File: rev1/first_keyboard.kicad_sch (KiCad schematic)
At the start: 79 parts, among them SW1 SW_Push, SW10 SW_Push, SW11 SW_Push, SW12 SW_Push, SW13 SW_Push, SW14 SW_Push, SW15 SW_Push, SW16 SW_Push, SW17 SW_Push, SW18 SW_Push, SW19 SW_Push, SW2 SW_Push, SW20 SW_Push, SW21 SW_Push, SW22 SW_Push, SW23 SW_Push, SW24 SW_Push, SW25 SW_Push, SW26 SW_Push, SW27 SW_Push, SW28 SW_Push, SW29 SW_Push, SW3 SW_Push, SW30 SW_Push, SW31 SW_Push, SW32 SW_Push, SW33 SW_Push, SW34 SW_Push, SW35 SW_Push, SW37 SW_Push, SW38 SW_Push, SW39 SW_Push, SW4 SW_Push, SW40 SW_Push, SW5 SW_Push, SW6 SW_Push, SW7 SW_Push, SW8 SW_Push, SW9 SW_Push, U1 RP2040

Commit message: feat: change rasp pico
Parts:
- removed U1: RP2040, Package_DFN_QFN:QFN-56-1EP_7x7mm_P0.4mm_EP3.2x3.2mm, symbol MCU_RaspberryPi:RP2040
- added U1: Pico, RPi_Pico:RPi_Pico_SMD_TH, symbol RPi_Pico:Pico

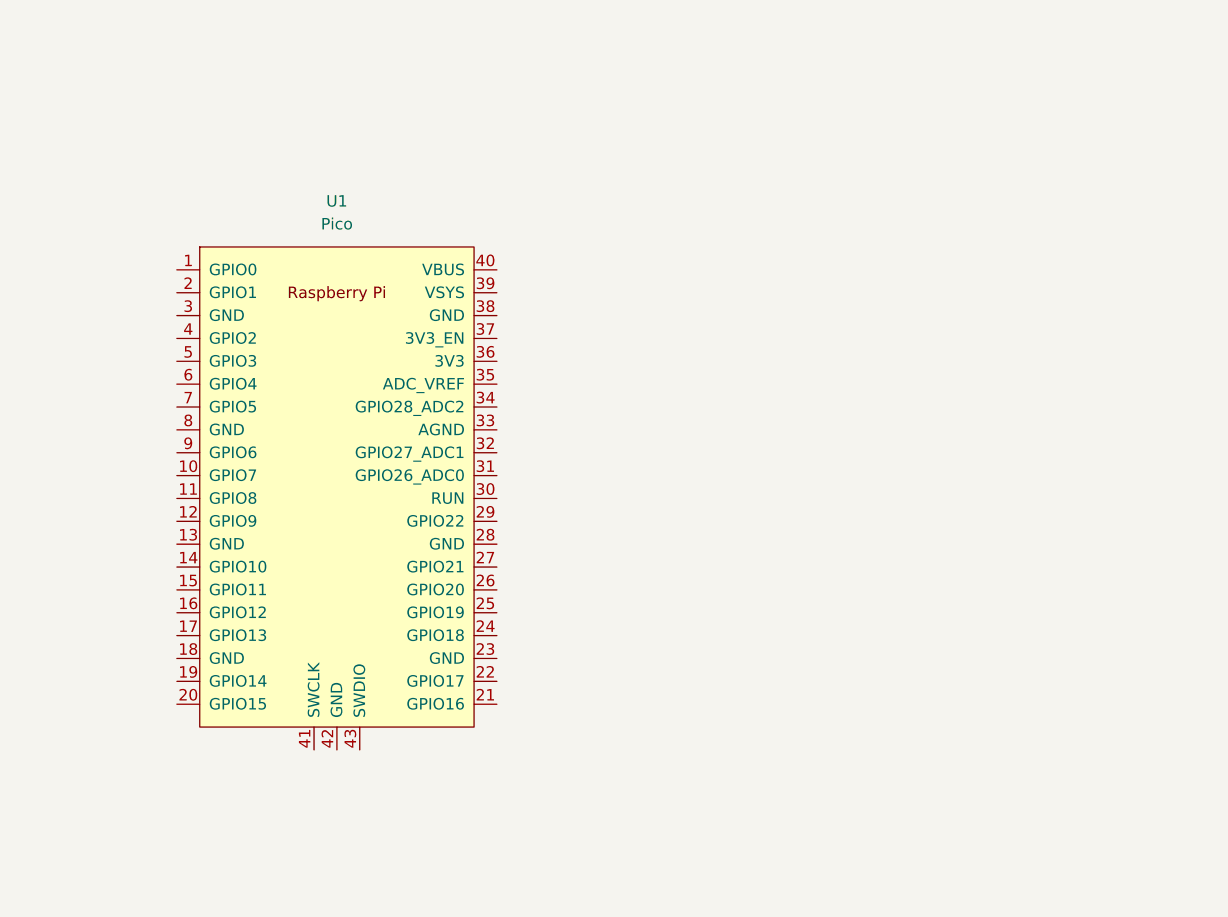
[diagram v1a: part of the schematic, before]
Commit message: feat: picoに配線した
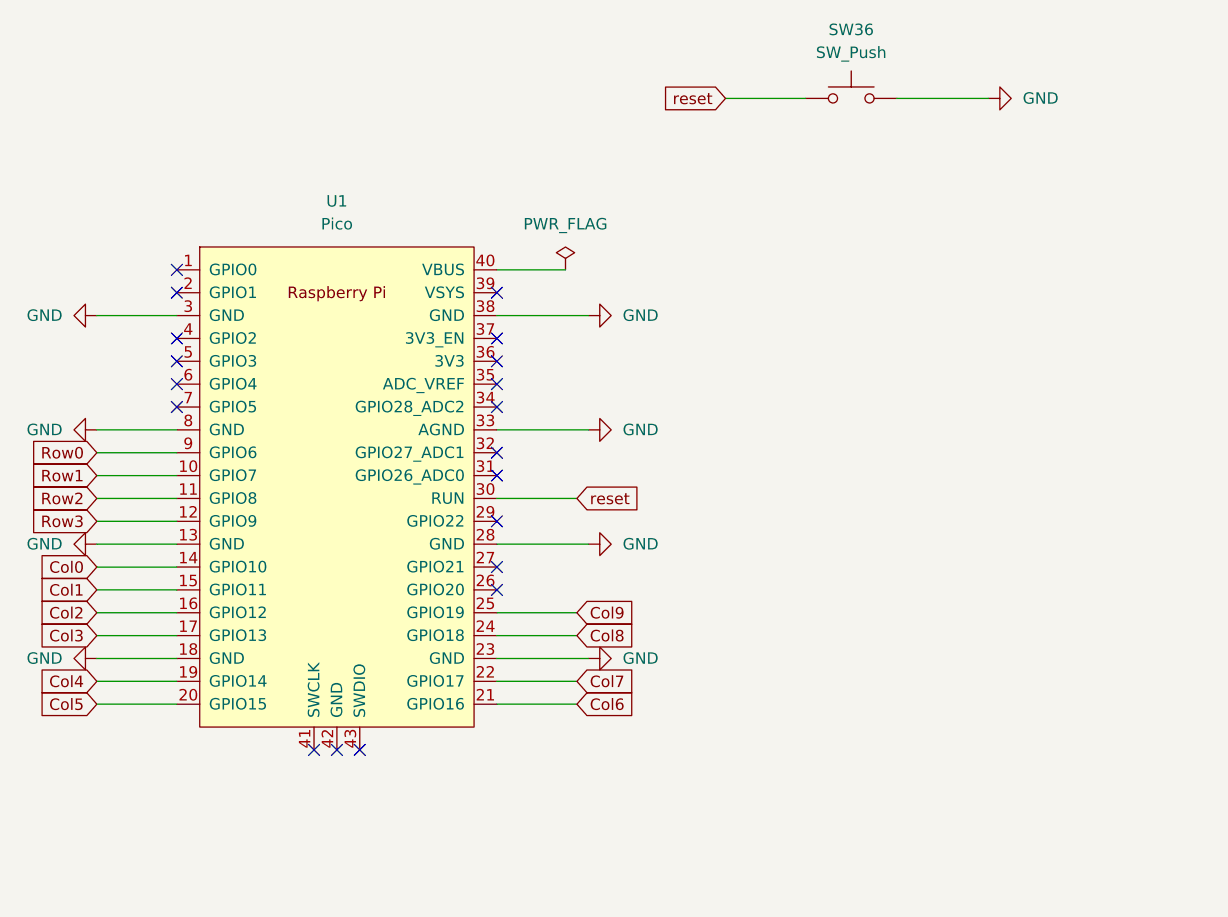
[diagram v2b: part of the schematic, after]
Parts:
- added SW36: SW_Push, symbol Switch:SW_Push
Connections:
- net Col0: now also U1.14 (GPIO10)
- net Col1: now also U1.15 (GPIO11)
- net Col2: now also U1.16 (GPIO12)
- net Col3: now also U1.17 (GPIO13)
- net Col4: now also U1.19 (GPIO14)
- net Col5: now also U1.20 (GPIO15)
- net Col6: now also U1.21 (GPIO16)
- net Col7: now also U1.22 (GPIO17)
- net Col8: now also U1.24 (GPIO18)
- net Col9: now also U1.25 (GPIO19)
- net Row0: now also U1.9 (GPIO6)
- net Row1: now also U1.10 (GPIO7)
- net Row2: now also U1.11 (GPIO8)
- net Row3: now also U1.12 (GPIO9)
- net GND: now reaches U1.13 (GND)
- net GND: now also U1.18 (GND), U1.23 (GND), U1.28 (GND), U1.3 (GND), U1.33 (AGND), U1.38 (GND), U1.8 (GND), SW36.2
- net reset: now reaches U1.30 (RUN)
- net reset: now also SW36.1
- no-connect marks 0 -> 19

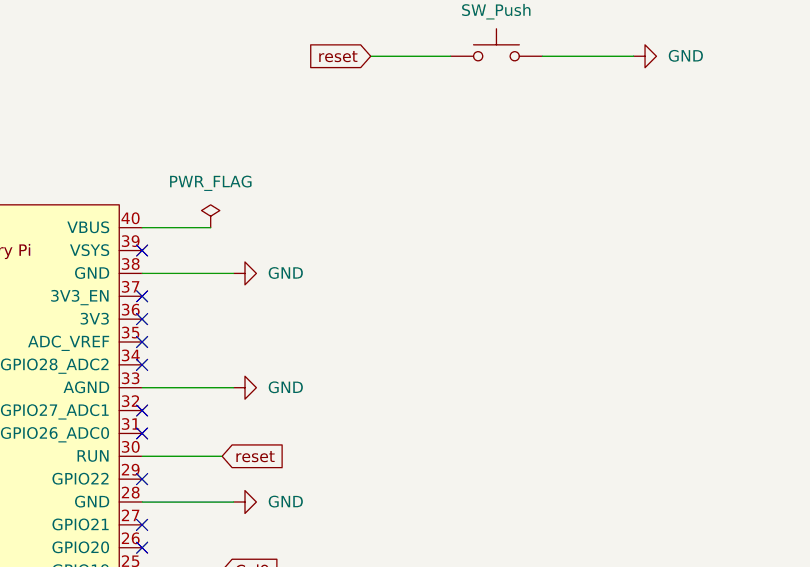
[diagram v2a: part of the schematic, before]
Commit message: feat: PWR_FLAG違反修正
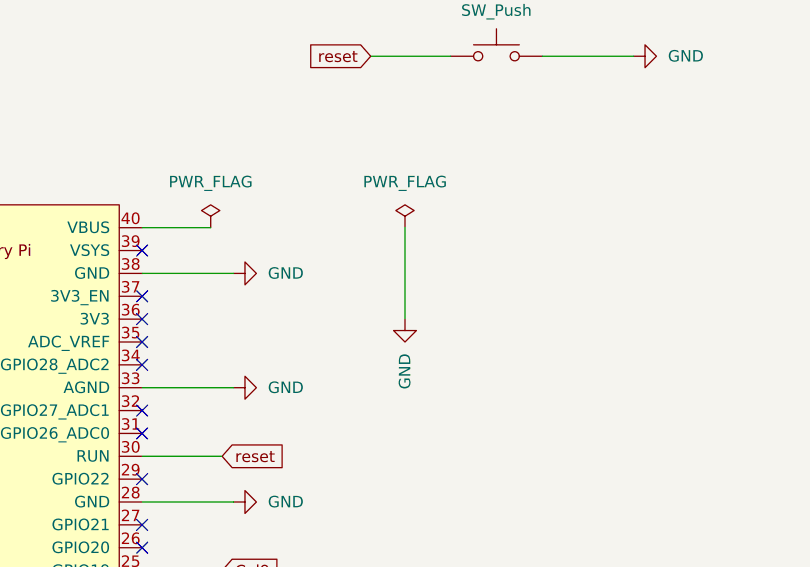
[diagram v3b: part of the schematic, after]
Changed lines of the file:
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@@
+    (stroke (width 0) (type default))
+  )
+  (wire (pts (xy 101.6 44.45) (xy 101.6 54.61))
     (stroke (width 0) (type default))
   )
@@
         (path "/30ce758a-13a8-4989-9c18-1386b25397ac"
           (reference "D1") (unit 1)
+        )
+      )
+    )
+  )
+  (symbol (lib_id "power:PWR_FLAG") (at 101.6 44.45 0) (unit 1)
+    (in_bom yes) (on_board yes) (dnp no) (fields_autoplaced)
+    (property "Reference" "#FLG02" (at 101.6 42.545 0)
+      (effects (font (size 1.27 1.27)) hide)
+    )
+    (property "Value" "PWR_FLAG" (at 101.6 39.37 0)
+      (effects (font (size 1.27 1.27)))
+    )
+    (property "Footprint" "" (at 101.6 44.45 0)
+      (effects (font (size 1.27 1.27)) hide)
+    )
+    (property "Datasheet" "~" (at 101.6 44.45 0)
+      (effects (font (size 1.27 1.27)) hide)
+    )
+    (pin "1")
+    (instances
+      (project "first_keyboard"
+        (path "/30ce758a-13a8-4989-9c18-1386b25397ac"
+          (reference "#FLG02") (unit 1)
         )
       )
@@
         )
       )
+    )
+  )
+  (symbol (lib_id "power:GND") (at 101.6 54.61 0) (unit 1)
+    (in_bom yes) (on_board yes) (dnp no) (fields_autoplaced)
+    (property "Reference" "#PWR010" (at 101.6 60.96 0)
+      (effects (font (size 1.27 1.27)) hide)
+    )
+    (property "Value" "GND" (at 101.6 58.42 90)
+      (effects (font (size 1.27 1.27)) (justify right))
+    )
+    (property "Footprint" "" (at 101.6 54.61 0)
+      (effects (font (size 1.27 1.27)) hide)
+    )
+    (property "Datasheet" "" (at 101.6 54.61 0)
+      (effects (font (size 1.27 1.27)) hide)
+    )
+    (pin "1")
+    (instances
+      (project "first_keyboard"
+        (path "/30ce758a-13a8-4989-9c18-1386b25397ac"
+          (reference "#PWR010") (unit 1)
+        )
+      )
